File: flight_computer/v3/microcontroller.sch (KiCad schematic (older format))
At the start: 27 parts, among them J1 Conn_01x05_Male, J2 Conn_01x05_Male, U34 MSP430FR5969IRGZR, U7 LT6654AHS6-3.3, Y1 CM8V-T1A

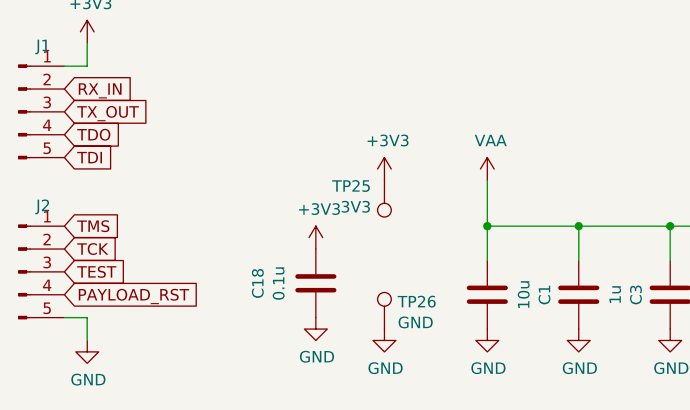
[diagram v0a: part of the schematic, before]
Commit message: Updating based on harnesses
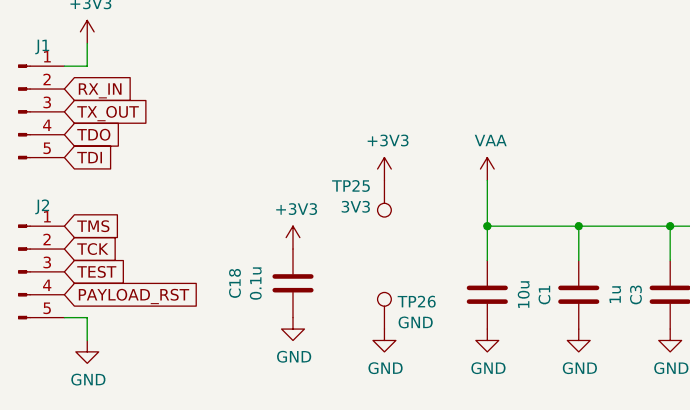
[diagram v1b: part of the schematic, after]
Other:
- moved on the sheet: C18
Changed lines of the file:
@@
 L Device:C C?
 U 1 1 6513B657
-P 2050 7200
+P 1950 7200
 AR Path="/6313FC31/6513B657" Ref="C?"  Part="1"
 AR Path="/6513B657" Ref="C?"  Part="1"
@@
 AR Path="/63D21EEE/6513B657" Ref="C?"  Part="1"
 AR Path="/64AE160A/6513B657" Ref="C18"  Part="1"
-F 0 "C18" V 2302 7200 50  0000 C CNN
-F 1 "0.1u" V 2211 7200 50  0000 C CNN
-F 2 "Capacitor_SMD:C_0603_1608Metric" H 2088 7050 50  0001 C CNN
-F 3 "~" H 2050 7200 50  0001 C CNN
-	1    2050 7200
+F 0 "C18" V 2202 7200 50  0000 C CNN
+F 1 "0.1u" V 2111 7200 50  0000 C CNN
+F 2 "Capacitor_SMD:C_0603_1608Metric" H 1988 7050 50  0001 C CNN
+F 3 "~" H 1950 7200 50  0001 C CNN
+	1    1950 7200
 	-1   0    0    1
 $EndComp
@@
 L power:GND #PWR?
 U 1 1 6513B65D
-P 2050 7350
+P 1950 7350
 AR Path="/6313FC31/6513B65D" Ref="#PWR?"  Part="1"
 AR Path="/6513B65D" Ref="#PWR?"  Part="1"
@@
 AR Path="/63D21EEE/6513B65D" Ref="#PWR?"  Part="1"
 AR Path="/64AE160A/6513B65D" Ref="#PWR0154"  Part="1"
-F 0 "#PWR0154" H 2050 7100 50  0001 C CNN
-F 1 "GND" H 2055 7177 50  0000 C CNN
-F 2 "" H 2050 7350 50  0001 C CNN
-F 3 "" H 2050 7350 50  0001 C CNN
-	1    2050 7350
+F 0 "#PWR0154" H 1950 7100 50  0001 C CNN
+F 1 "GND" H 1955 7177 50  0000 C CNN
+F 2 "" H 1950 7350 50  0001 C CNN
+F 3 "" H 1950 7350 50  0001 C CNN
+	1    1950 7350
 	1    0    0    -1
 $EndComp
@@
 L power:+3V3 #PWR?
 U 1 1 6513C640
-P 2050 7050
+P 1950 7050
 AR Path="/6513C640" Ref="#PWR?"  Part="1"
 AR Path="/63D1F518/6513C640" Ref="#PWR?"  Part="1"
 AR Path="/63D21EEE/6513C640" Ref="#PWR?"  Part="1"
 AR Path="/64AE160A/6513C640" Ref="#PWR0158"  Part="1"
-F 0 "#PWR0158" H 2050 6900 50  0001 C CNN
-F 1 "+3V3" H 2065 7223 50  0000 C CNN
-F 2 "" H 2050 7050 50  0001 C CNN
-F 3 "" H 2050 7050 50  0001 C CNN
-	1    2050 7050
+F 0 "#PWR0158" H 1950 6900 50  0001 C CNN
+F 1 "+3V3" H 1965 7223 50  0000 C CNN
+F 2 "" H 1950 7050 50  0001 C CNN
+F 3 "" H 1950 7050 50  0001 C CNN
+	1    1950 7050
 	1    0    0    -1
 $EndComp

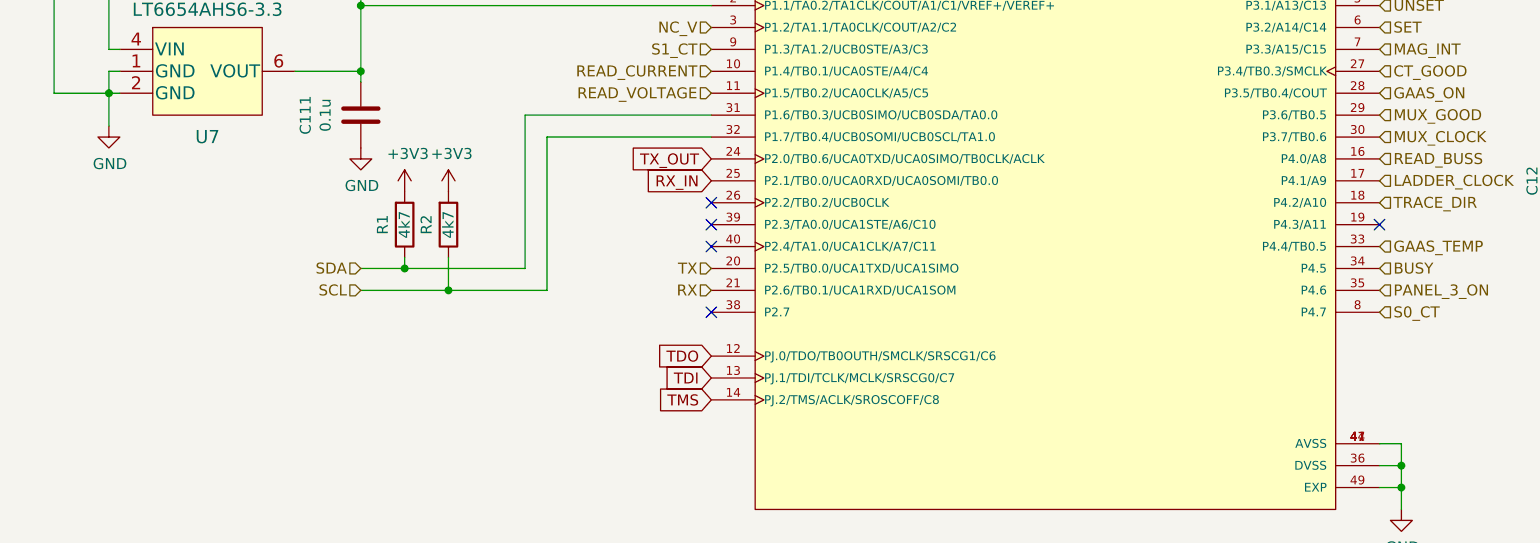
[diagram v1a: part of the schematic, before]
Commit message: Update hardware
- Add separate discharge resistance paths to flight computer
- Update footprint for payload holder
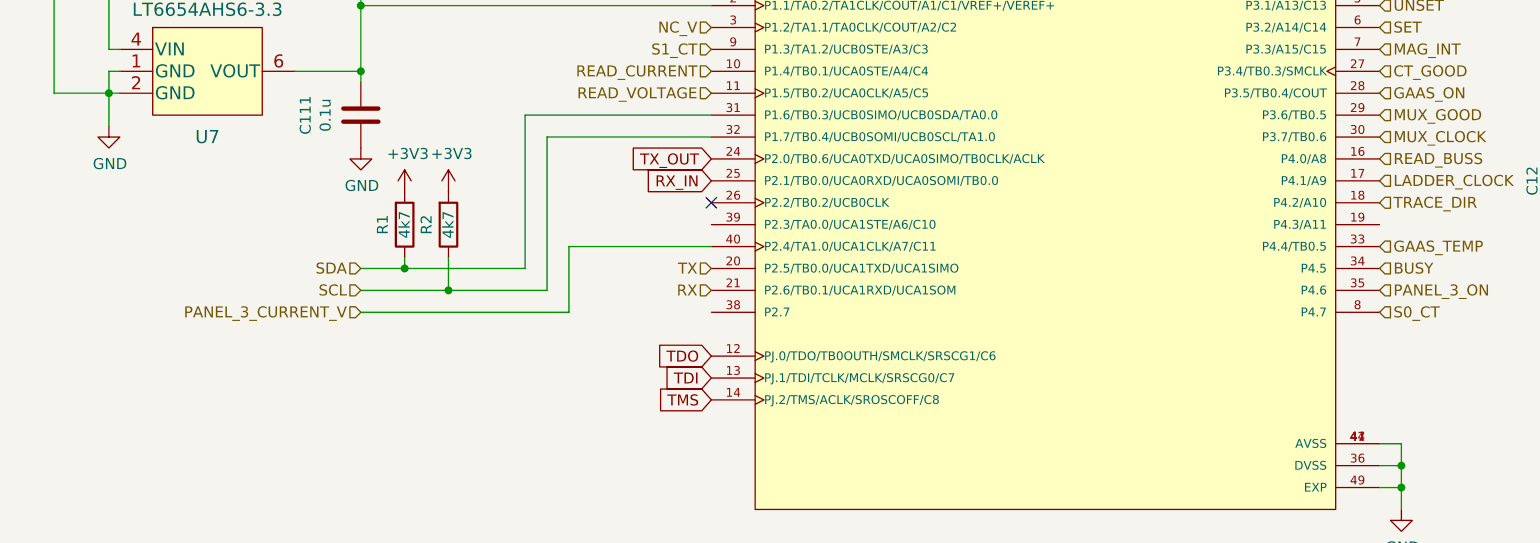
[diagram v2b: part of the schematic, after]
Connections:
- net PANEL_3_CURRENT_V: now reaches U34.40 (P2.4/TA1.0/UCA1CLK/A7/C11)
- no-connect marks 7 -> 3
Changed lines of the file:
@@
 Text GLabel 950  7150 2    50   Input ~ 0
 TEST
-NoConn ~ 7700 4100
-NoConn ~ 4650 4500
 NoConn ~ 4650 4000
-NoConn ~ 4650 4100
-NoConn ~ 4650 4200
+Text HLabel 3050 4500 0    50   Input ~ 0
+PANEL_3_CURRENT_V
+Wire Wire Line
+	3050 4500 4000 4500
+Wire Wire Line
+	4000 4500 4000 4200
+Wire Wire Line
+	4000 4200 4650 4200
 $EndSCHEMATC

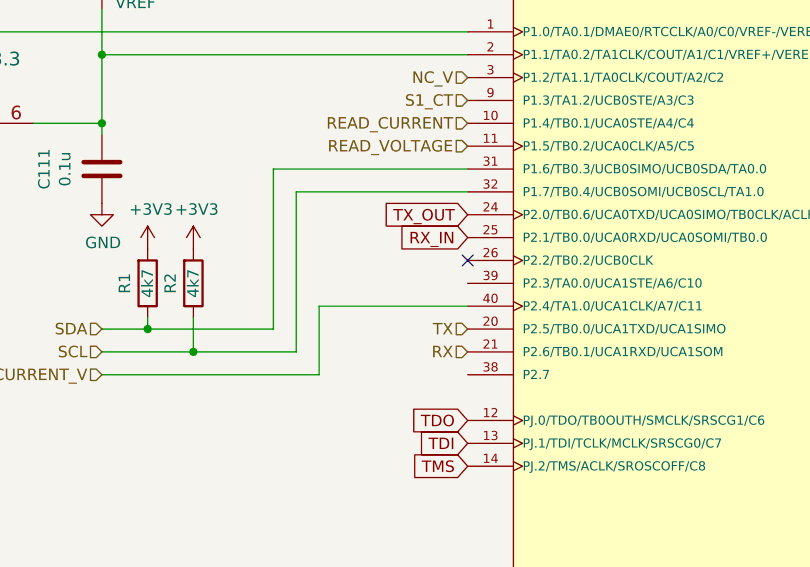
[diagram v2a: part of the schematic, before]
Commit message: Finished PCBs
- Finished flight computer
- Finished payload holder
- Finished contact board
- Ordered everything
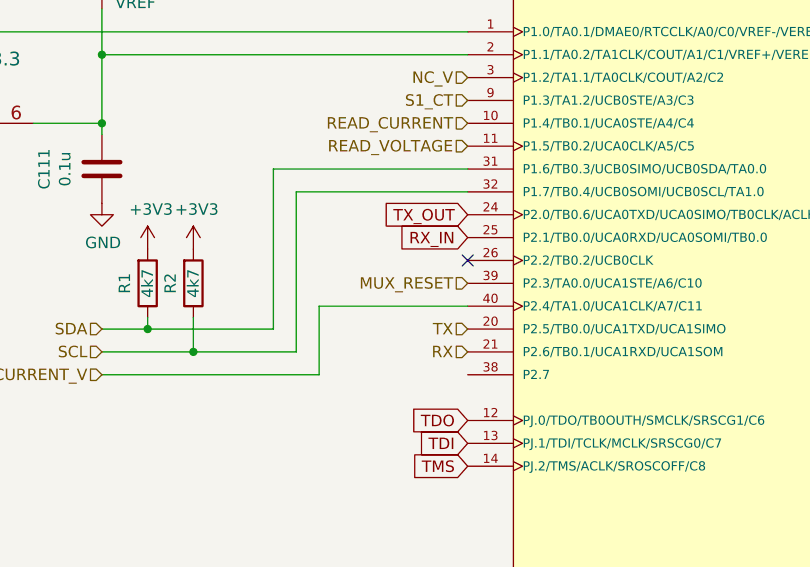
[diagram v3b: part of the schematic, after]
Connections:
- net MUX_RESET: now reaches U34.39 (P2.3/TA0.0/UCA1STE/A6/C10)
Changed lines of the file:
@@
 Wire Wire Line
 	4000 4200 4650 4200
+Text HLabel 4650 4100 0    50   Input ~ 0
+MUX_RESET
 $EndSCHEMATC

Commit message: Update flight computer
- Add exposed pad to microcontroller
- Update flight computer firmware
- Update secondary payload outline
- Order boards
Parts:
- U34: footprint Package_QFP:LQFP-48_7x7mm_P0.5mm -> Package_QFP:LQFP-48-1EP_7x7mm_P0.5mm_EP3.6x3.6mm
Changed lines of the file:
@@
 F 0 "U8" H 6175 5565 50  0000 C CNN
 F 1 "MSP430FR5969IRGZR" H 6175 5474 50  0000 C CNN
-F 2 "Package_QFP:LQFP-48_7x7mm_P0.5mm" H 6600 3700 50  0001 L BNN
+F 2 "Package_QFP:LQFP-48-1EP_7x7mm_P0.5mm_EP3.6x3.6mm" H 6600 3700 50  0001 L BNN
 F 3 "" H 6600 3700 50  0001 L BNN
 	1    6200 3700
